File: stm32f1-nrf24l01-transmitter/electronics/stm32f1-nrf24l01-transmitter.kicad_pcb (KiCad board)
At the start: 2 copper layers, 28 parts, among them K1 CONN_3, K10 CONN_3, K11 CONN_3, K12 CONN_3, K2 CONN_3, K3 CONN_3, K4 CONN_3, K5 CONN_3, K6 CONN_3, K7 CONN_3, K8 CONN_3, K9 CONN_3, P1 Charge, P2 LED, P3 CONN_2, P4 CONN_2, Q1 BC548, SW1 ON/OFF, U1 LIPO_CHARGER_+_PROTECTION, U2 STM32F103C8T6_DEV_BOARD, U3 NRF24L01P

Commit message: Tweak schematics
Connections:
- U2 pad 20: (no net) -> N-0000031
- U2 pad 21: (no net) -> N-0000031
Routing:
- net N-0000031: track 0.00 -> 15.2 mm

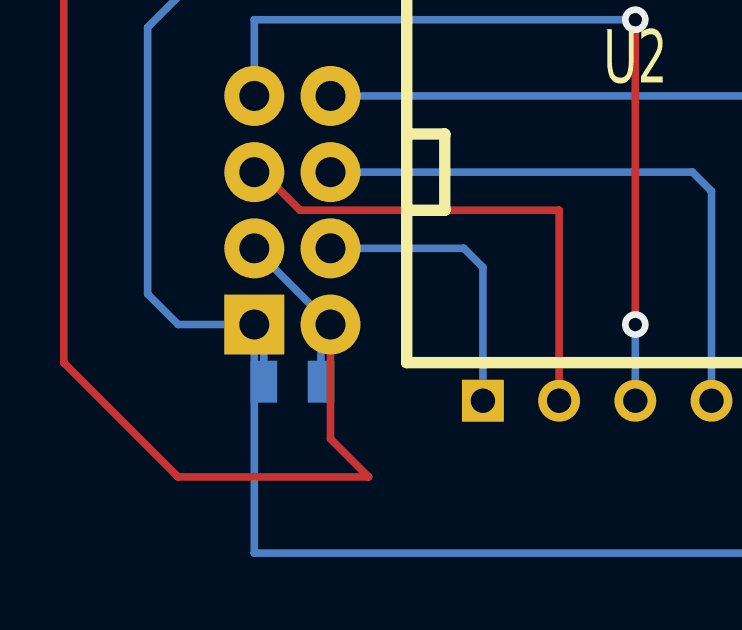
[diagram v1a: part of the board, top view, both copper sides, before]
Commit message: Make CE pin software controllable
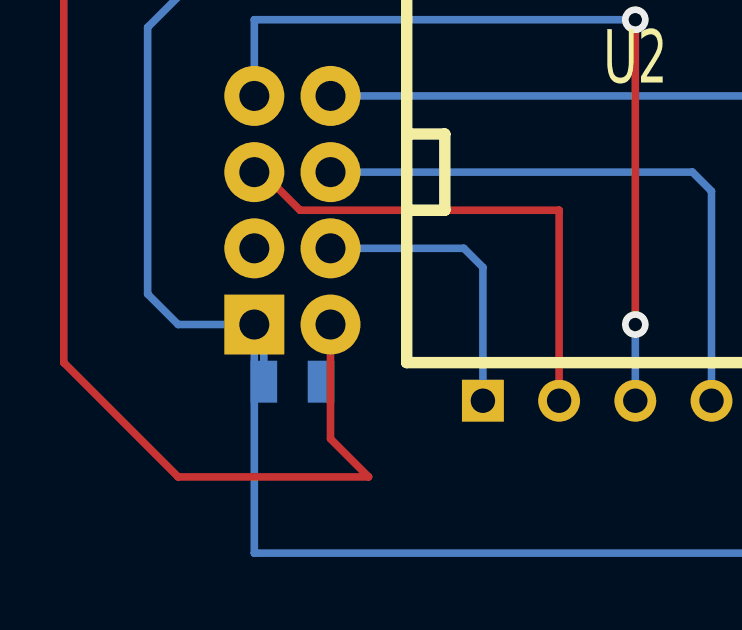
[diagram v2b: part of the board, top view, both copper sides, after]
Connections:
- C1 pad 1: VCC -> (no net)
- U2 pad 11: (no net) -> /CE
- U3 pad 3: VCC -> /CE
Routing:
- net VCC: track 112.2 -> 106.6 mm

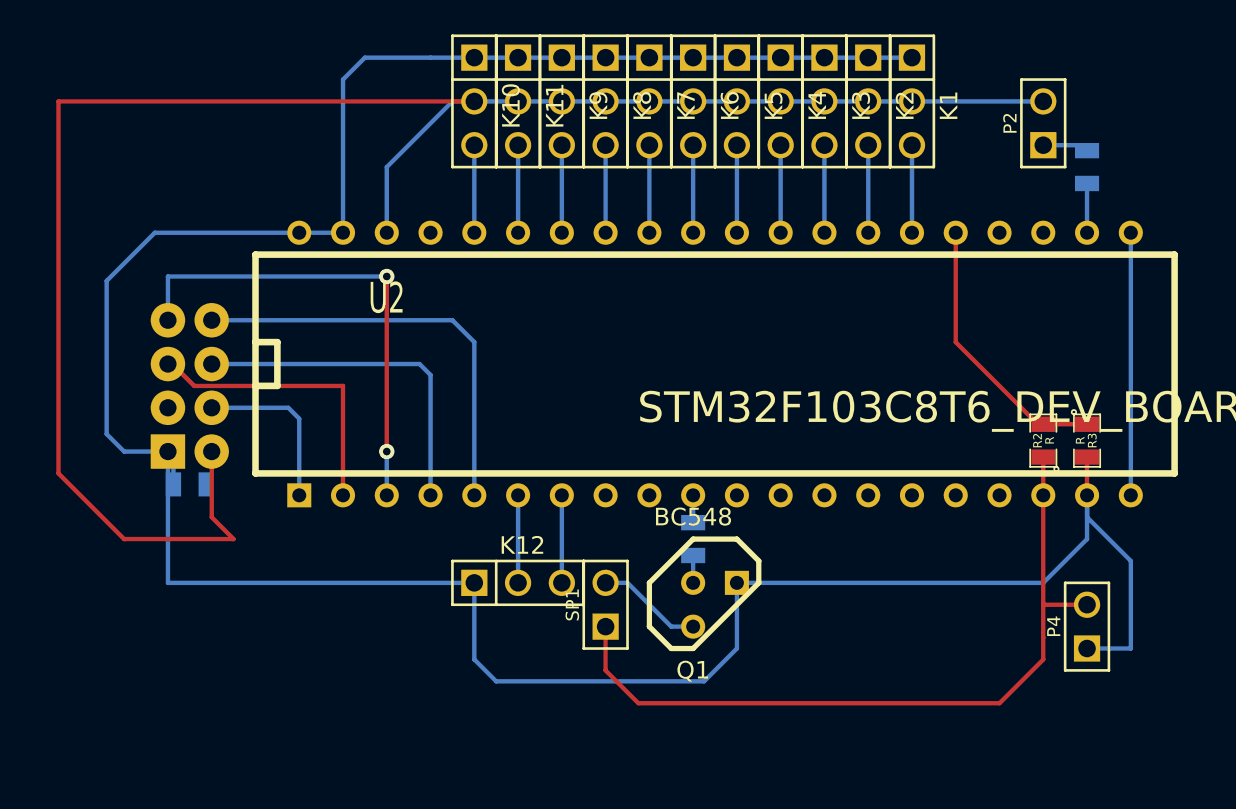
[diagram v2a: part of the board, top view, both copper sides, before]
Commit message: nRF24L01 CE tied to Vcc; Add smoothing cap for battery measurement
Add 4-pin socket for BT module
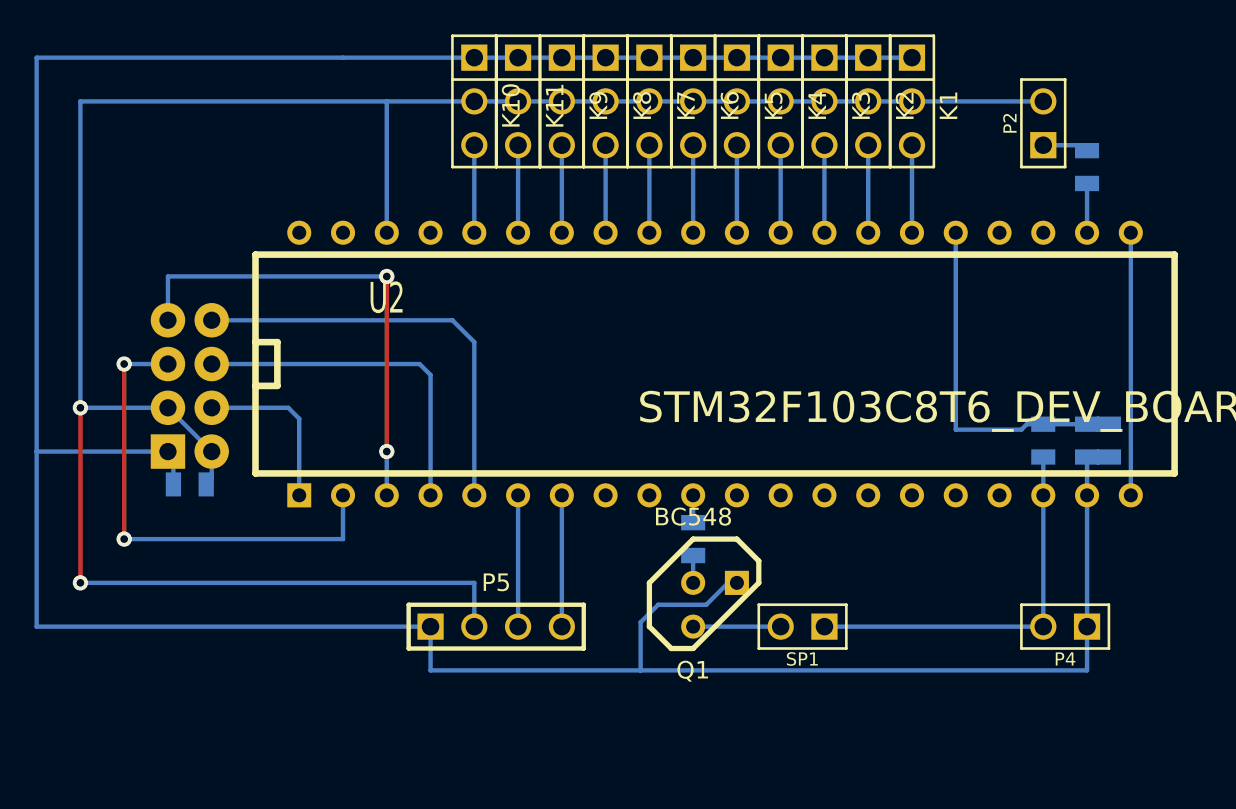
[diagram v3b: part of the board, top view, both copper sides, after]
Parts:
- removed K12: CONN_3, PIN_ARRAY_3X1
- added C2: 100nF, SM0805, B.Cu at (273.1, 128.9)
- added P5: CONN_4, PIN_ARRAY_4x1, F.Cu at (237.5, 139.7)
- R2, R3: moved to B.Cu
- moved SP1 11.5 mm to (255.3, 139.7), turned to 180 degrees
- moved P4 1.27 mm to (270.5, 139.7), turned to 180 degrees
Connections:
- C1 pad 1: (no net) -> VCC
- U2 pad 11: /CE -> (no net)
- U3 pad 3: /CE -> VCC
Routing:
- net VDD: track 44.1 -> 22.5 mm
- net VCC: track 106.6 -> 127.5 mm, vias 0 -> 2
- net GND: track 161.0 -> 180.0 mm
- net /SCK: track 17.0 -> 27.9 mm, vias 0 -> 2
- net /ADC0: track 15.9 -> 20.5 mm
- net /TX: track 5.08 -> 7.62 mm
- net /RX: track 5.08 -> 7.62 mm
- net N-0000014: track 6.13 -> 5.08 mm

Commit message: Optimize layout
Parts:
- moved SP1 8.03 mm to (262.9, 137.2)
- moved P4 2.54 mm to (270.5, 137.2)
- moved P5 2.54 mm to (237.5, 137.2)
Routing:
- net GND: track 180.0 -> 122.4 mm, vias 0 -> 4
- net VDD: track 22.5 -> 12.4 mm
- net N-0000014: track 5.08 -> 15.2 mm
- net VCC: track 127.5 -> 122.5 mm
- net /SCK: track 27.9 -> 33.0 mm
- net /TX: track 7.62 -> 5.08 mm
- net /RX: track 7.62 -> 5.08 mm

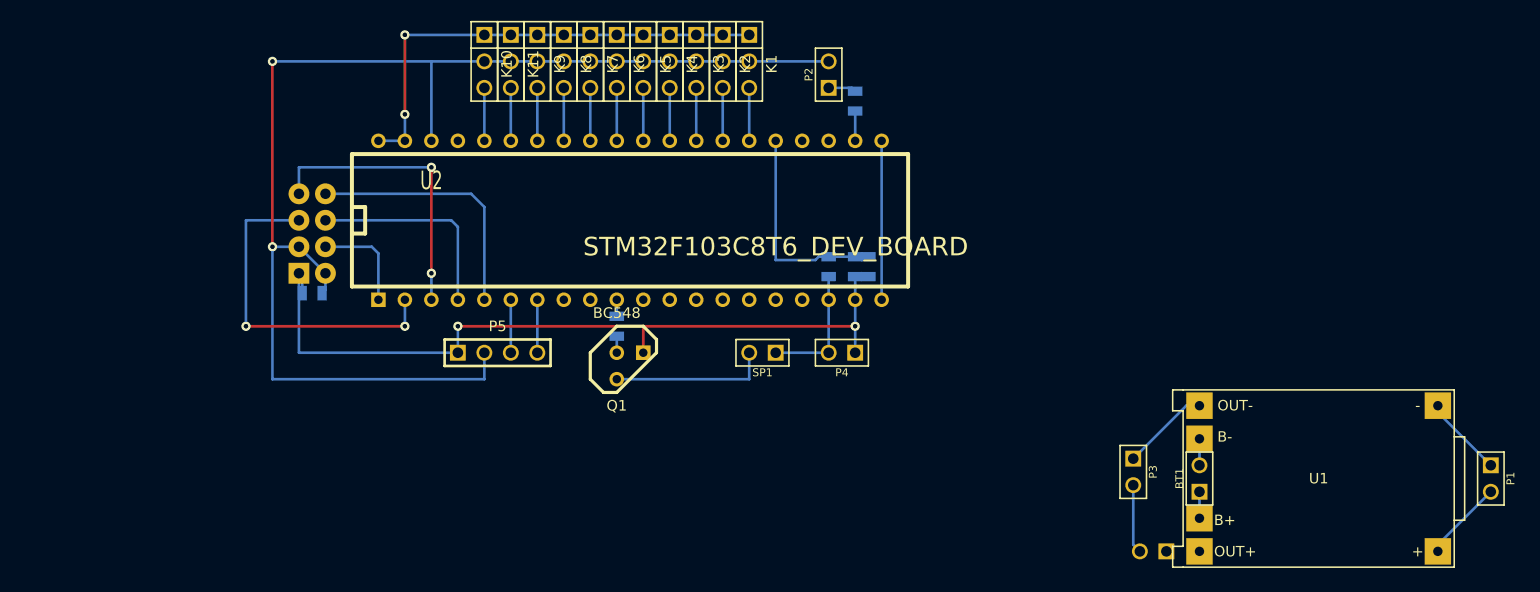
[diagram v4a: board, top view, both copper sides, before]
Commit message: Annotate the PCB and increase track widths for better visibility
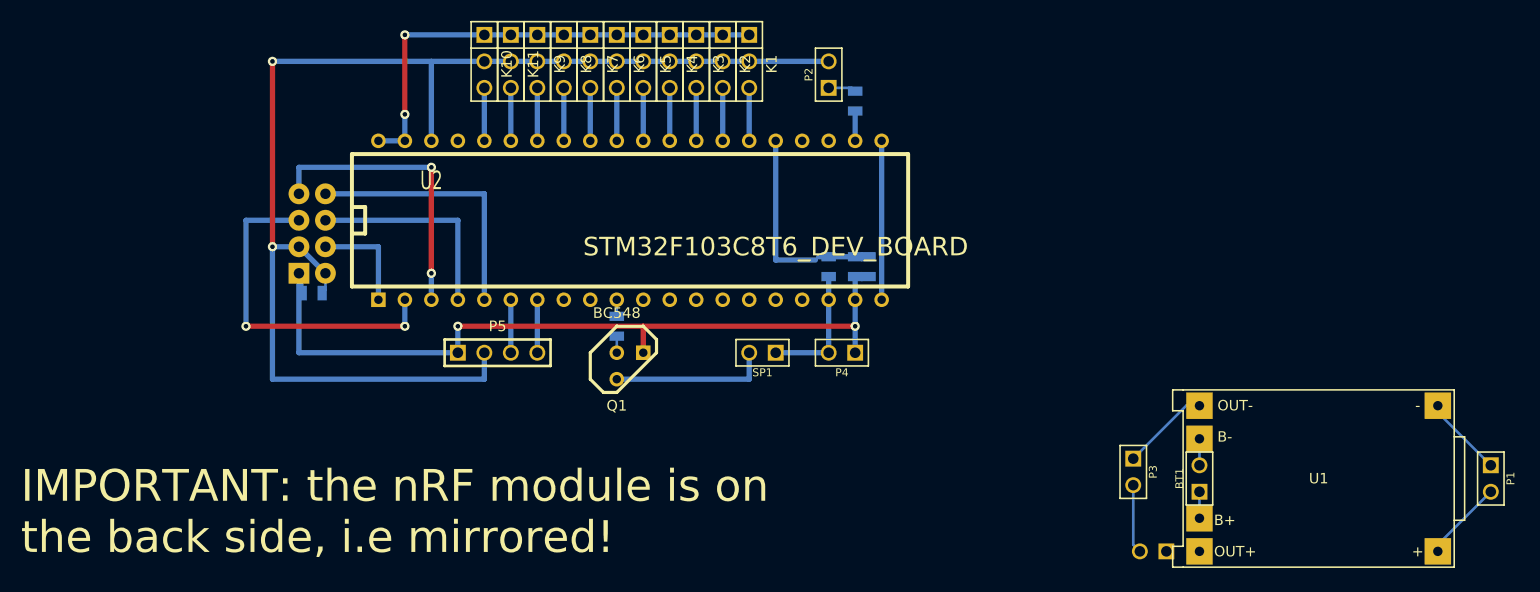
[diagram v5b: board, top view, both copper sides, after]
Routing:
- net /IRQ: track 24.7 -> 25.4 mm
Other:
- board text added: "IMPORTANT: the nRF module is on the back side, i.e mirrored!"
